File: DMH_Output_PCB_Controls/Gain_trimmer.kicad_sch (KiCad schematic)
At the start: 8 parts, among them U8 TL074

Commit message: Starting Controls PCB design
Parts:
- added J11: Conn_01x06, Connector_PinSocket_2.54mm:PinSocket_1x06_P2.54mm_Vertical, symbol Connector_Generic:Conn_01x06
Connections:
- net L_Gain_IN: now also J11.3 (Pin_3)
- net L_Gain_OUT: now also J11.1 (Pin_1)
- net R_Gain_IN: now also J11.6 (Pin_6)
- net R_Gain_OUT: now also J11.4 (Pin_4)
- net at RV1.5, U8.12 (+): now also J11.5 (Pin_5)
- net at RV1.2, U8.3 (+): now also J11.2 (Pin_2)

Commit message: Controls PCB placement ongoing
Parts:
- RV1: Function (none) -> Volume
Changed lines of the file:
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@@
 		(exclude_from_sim no)
 		(in_bom yes)
-		(on_board yes)
+		(on_board no)
 		(dnp no)
 		(property "Reference" "U8"
@@
 		(exclude_from_sim no)
 		(in_bom yes)
-		(on_board yes)
+		(on_board no)
 		(dnp no)
 		(fields_autoplaced yes)
@@
 		(exclude_from_sim no)
 		(in_bom yes)
-		(on_board yes)
+		(on_board no)
 		(dnp no)
 		(property "Reference" "U8"
@@
 			)
 		)
-		(property "Function" ""
+		(property "Function" "Volume"
 			(at 76.2 50.8 0)
 			(effects
 				(font
 					(size 1.27 1.27)
-				)
+					(thickness 0.254)
+					(bold yes)
+					(italic yes)
+				)
+				(hide yes)
 			)
 		)
@@
 		(exclude_from_sim no)
 		(in_bom yes)
-		(on_board yes)
+		(on_board no)
 		(dnp no)
 		(property "Reference" "U8"
@@
 		(exclude_from_sim no)
 		(in_bom yes)
-		(on_board yes)
+		(on_board no)
 		(dnp no)
 		(fields_autoplaced yes)
@@
 		(exclude_from_sim no)
 		(in_bom yes)
-		(on_board yes)
+		(on_board no)
 		(dnp no)
 		(fields_autoplaced yes)
@@
 		(exclude_from_sim no)
 		(in_bom yes)
-		(on_board yes)
+		(on_board no)
 		(dnp no)
 		(fields_autoplaced yes)
@@
 		(exclude_from_sim no)
 		(in_bom yes)
-		(on_board yes)
+		(on_board no)
 		(dnp no)
 		(fields_autoplaced yes)
@@
 		(exclude_from_sim no)
 		(in_bom yes)
-		(on_board yes)
+		(on_board no)
 		(dnp no)
 		(fields_autoplaced yes)
@@
 		(exclude_from_sim no)
 		(in_bom yes)
-		(on_board yes)
+		(on_board no)
 		(dnp no)
 		(fields_autoplaced yes)
@@
 		(exclude_from_sim no)
 		(in_bom yes)
-		(on_board yes)
+		(on_board no)
 		(dnp no)
 		(fields_autoplaced yes)
@@
 		(exclude_from_sim no)
 		(in_bom yes)
-		(on_board yes)
+		(on_board no)
 		(dnp no)
 		(property "Reference" "U8"
@@
 			)
 		)
-		(property "Function" ""
+		(property "Function" "Volume"
 			(at 76.2 114.3 0)
 			(effects
 				(font
 					(size 1.27 1.27)
-				)
-			)
-		)
+					(thickness 0.254)
+					(bold yes)
+					(italic yes)
+				)
+				(hide yes)
+			)
+		)

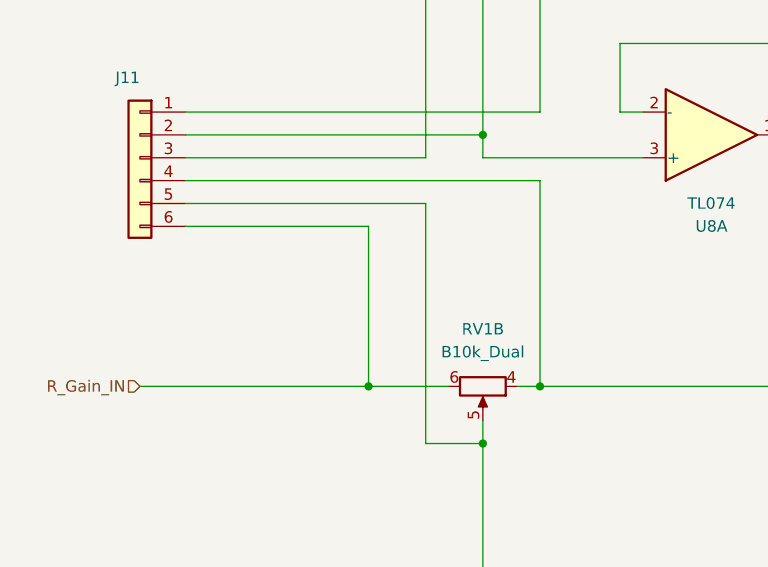
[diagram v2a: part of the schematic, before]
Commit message: Controls PCB comp placement done
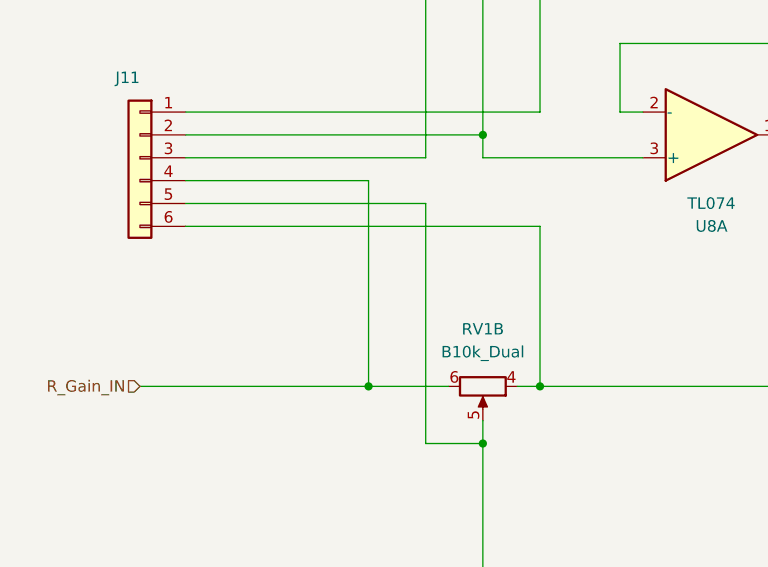
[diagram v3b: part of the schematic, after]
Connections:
- net R_Gain_IN: now also J11.4 (Pin_4); no longer J11.6 (Pin_6)
- net R_Gain_OUT: now also J11.6 (Pin_6); no longer J11.4 (Pin_4)
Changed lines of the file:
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@@
 	(wire
 		(pts
-			(xy 43.18 91.44) (xy 82.55 91.44)
+			(xy 43.18 96.52) (xy 82.55 96.52)
 		)
 		(stroke
@@
 	(wire
 		(pts
+			(xy 43.18 91.44) (xy 63.5 91.44)
+		)
+		(stroke
+			(width 0)
+			(type default)
+		)
+	)
+	(wire
+		(pts
 			(xy 149.86 114.3) (xy 149.86 127)
 		)
@@
 	(wire
 		(pts
-			(xy 82.55 91.44) (xy 82.55 114.3)
-		)
-		(stroke
-			(width 0)
-			(type default)
-		)
-	)
-	(wire
-		(pts
 			(xy 76.2 120.65) (xy 76.2 152.4)
 		)
@@
 	(wire
 		(pts
+			(xy 63.5 91.44) (xy 63.5 114.3)
+		)
+		(stroke
+			(width 0)
+			(type default)
+		)
+	)
+	(wire
+		(pts
 			(xy 129.54 127) (xy 129.54 139.7)
 		)
@@
 	(wire
 		(pts
-			(xy 63.5 96.52) (xy 63.5 114.3)
-		)
-		(stroke
-			(width 0)
-			(type default)
-		)
-	)
-	(wire
-		(pts
-			(xy 43.18 96.52) (xy 63.5 96.52)
-		)
-		(stroke
-			(width 0)
-			(type default)
-		)
-	)
-	(wire
-		(pts
 			(xy 69.85 120.65) (xy 76.2 120.65)
 		)
@@
 		)
 		(stroke
+			(width 0)
+			(type default)
+		)
+	)
+	(wire
+		(pts
+			(xy 82.55 96.52) (xy 82.55 114.3)
+		)
+		(stroke

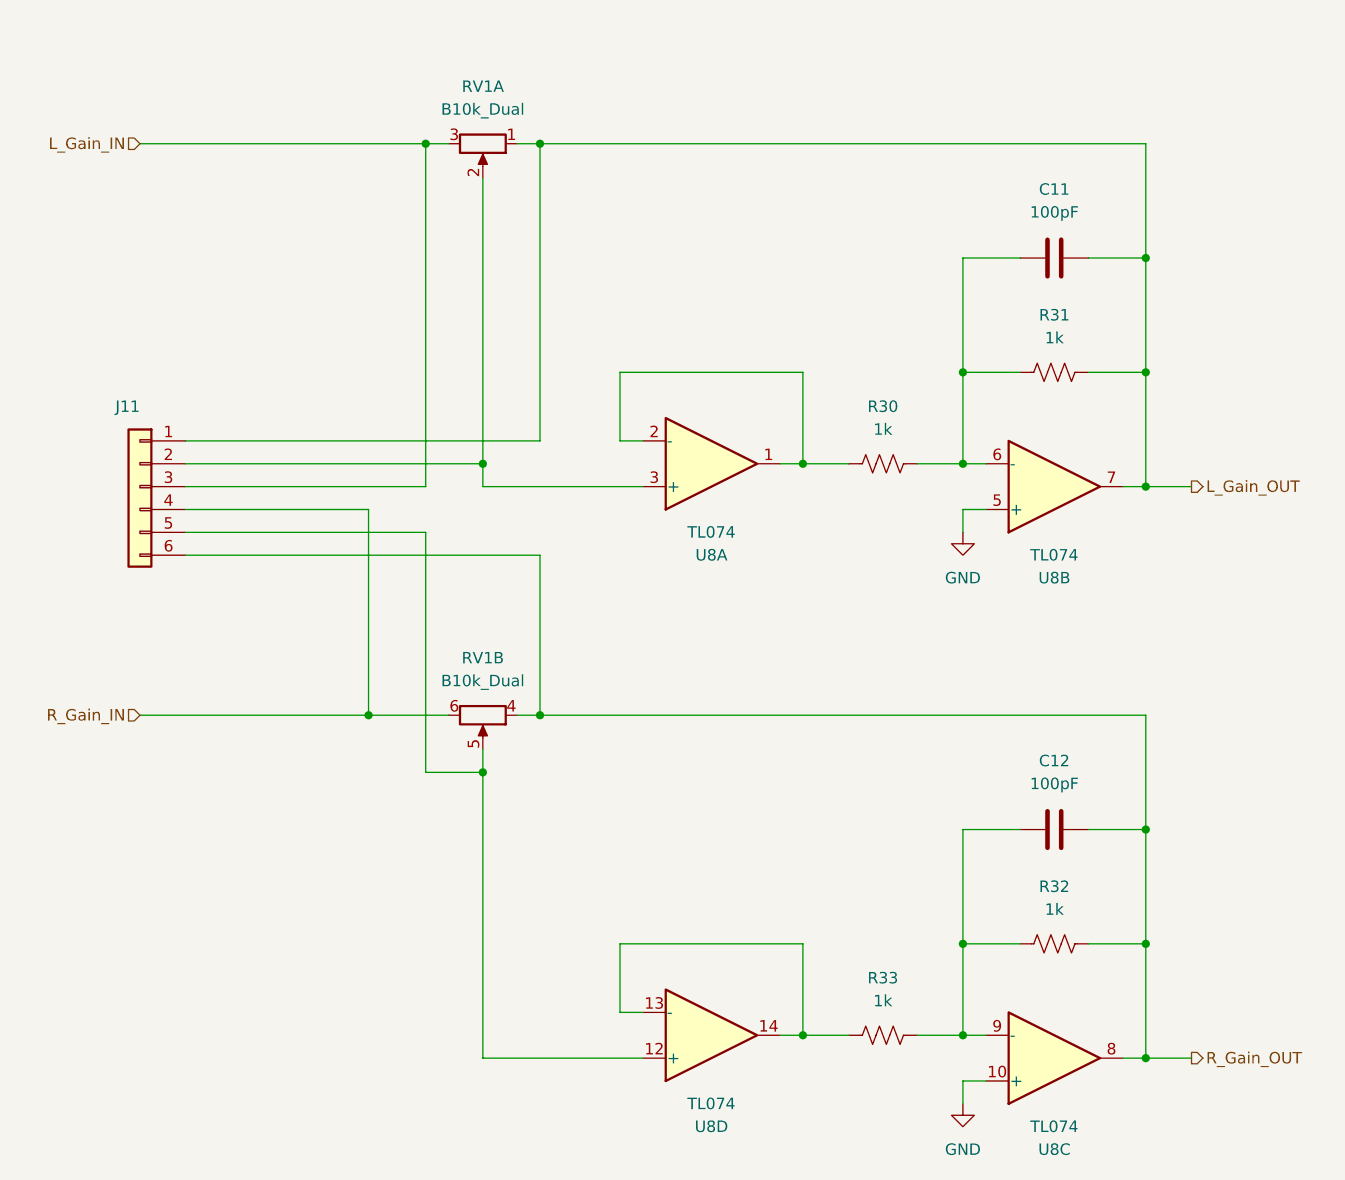
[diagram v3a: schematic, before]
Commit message: Clarifying inter PCB connectors in progress
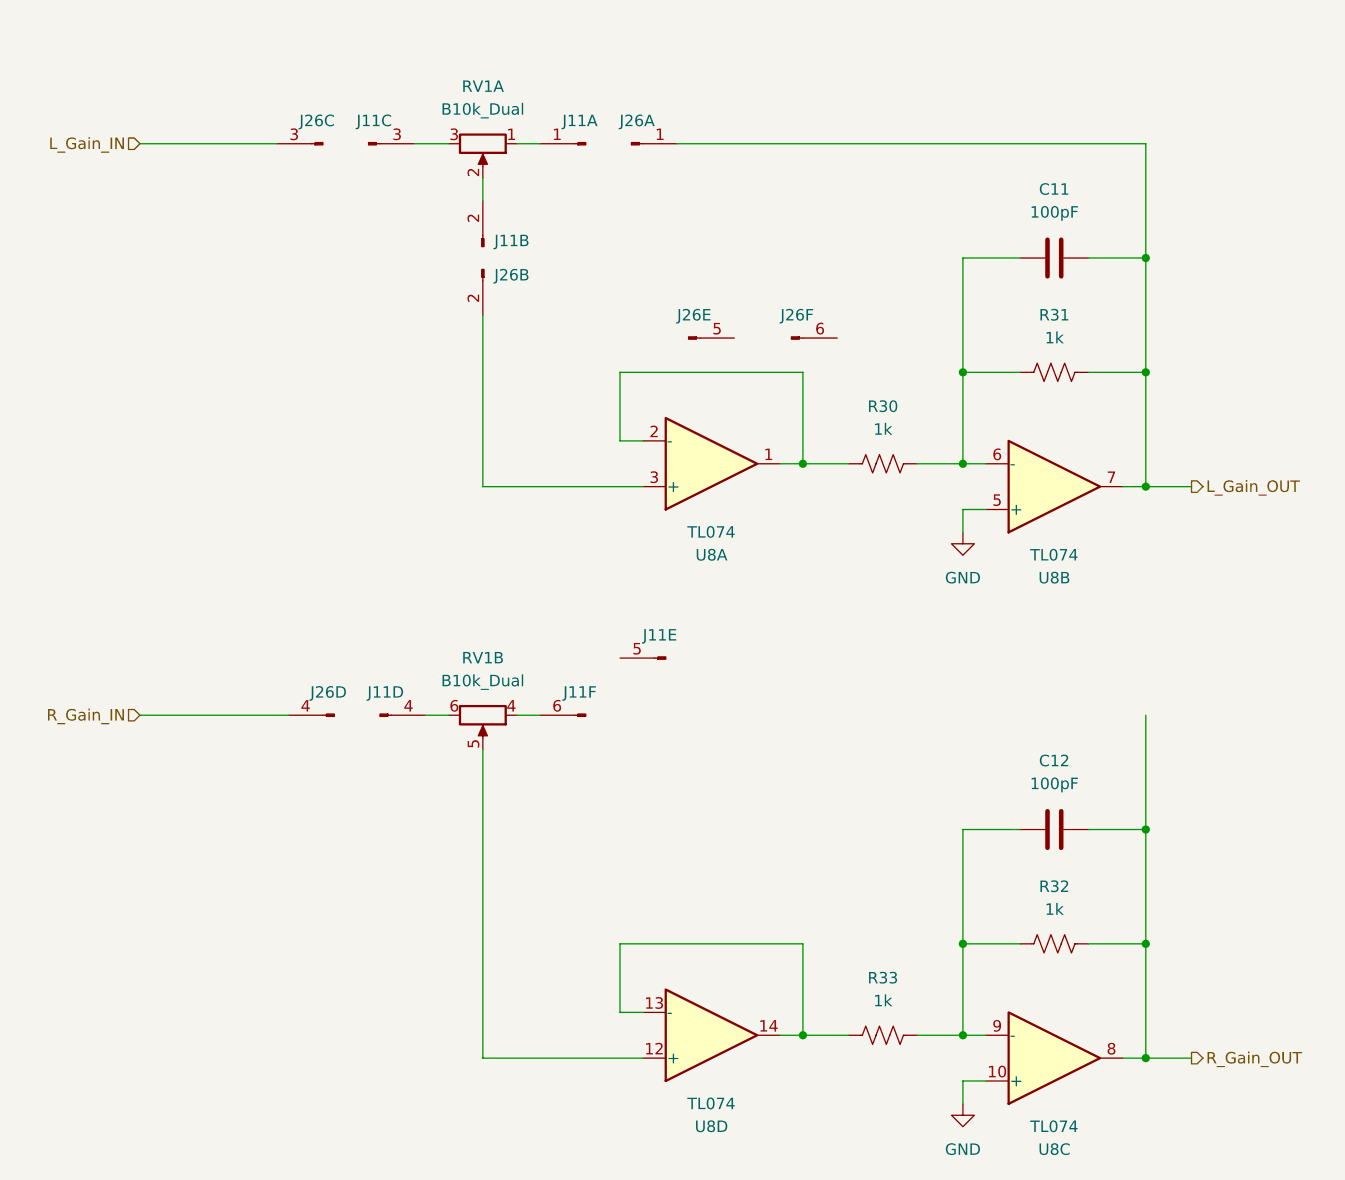
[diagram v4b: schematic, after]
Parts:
- removed J11: Conn_01x06, Connector_PinSocket_2.54mm:PinSocket_1x06_P2.54mm_Vertical, symbol Connector_Generic:Conn_01x06
- added J11: Conn_01x06_PinHeader, Connector_PinSocket_2.54mm:PinSocket_1x06_P2.54mm_Vertical, symbol SynthStuff:Conn_01x06_PinHeader
- added J26: Conn_01x06_PinHeader, Connector_PinHeader_2.54mm:PinHeader_1x06_P2.54mm_Vertical, symbol SynthStuff:Conn_01x06_PinHeader
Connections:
- net L_Gain_IN: now also J26.3 (Pin_3); no longer RV1.3
- net L_Gain_OUT: now also J26.1 (Pin_1); no longer RV1.1
- net R_Gain_IN: now also J26.4 (Pin_4); no longer RV1.6
- net R_Gain_OUT: no longer RV1.4
- net at U8.3 (+): now also J26.2 (Pin_2); no longer RV1.2
- new net: J11.1 (Pin_1), RV1.1
- new net: J11.2 (Pin_2), RV1.2
- new net: J11.3 (Pin_3), RV1.3
- new net: J11.6 (Pin_6), RV1.4
- new net: J11.4 (Pin_4), RV1.6
